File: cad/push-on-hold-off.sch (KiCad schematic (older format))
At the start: 13 parts, among them P1 CONN_01X04, P2 CONN_01X04, Q1 IRF7309IPBF, SW1 SW_PUSH_SMALL

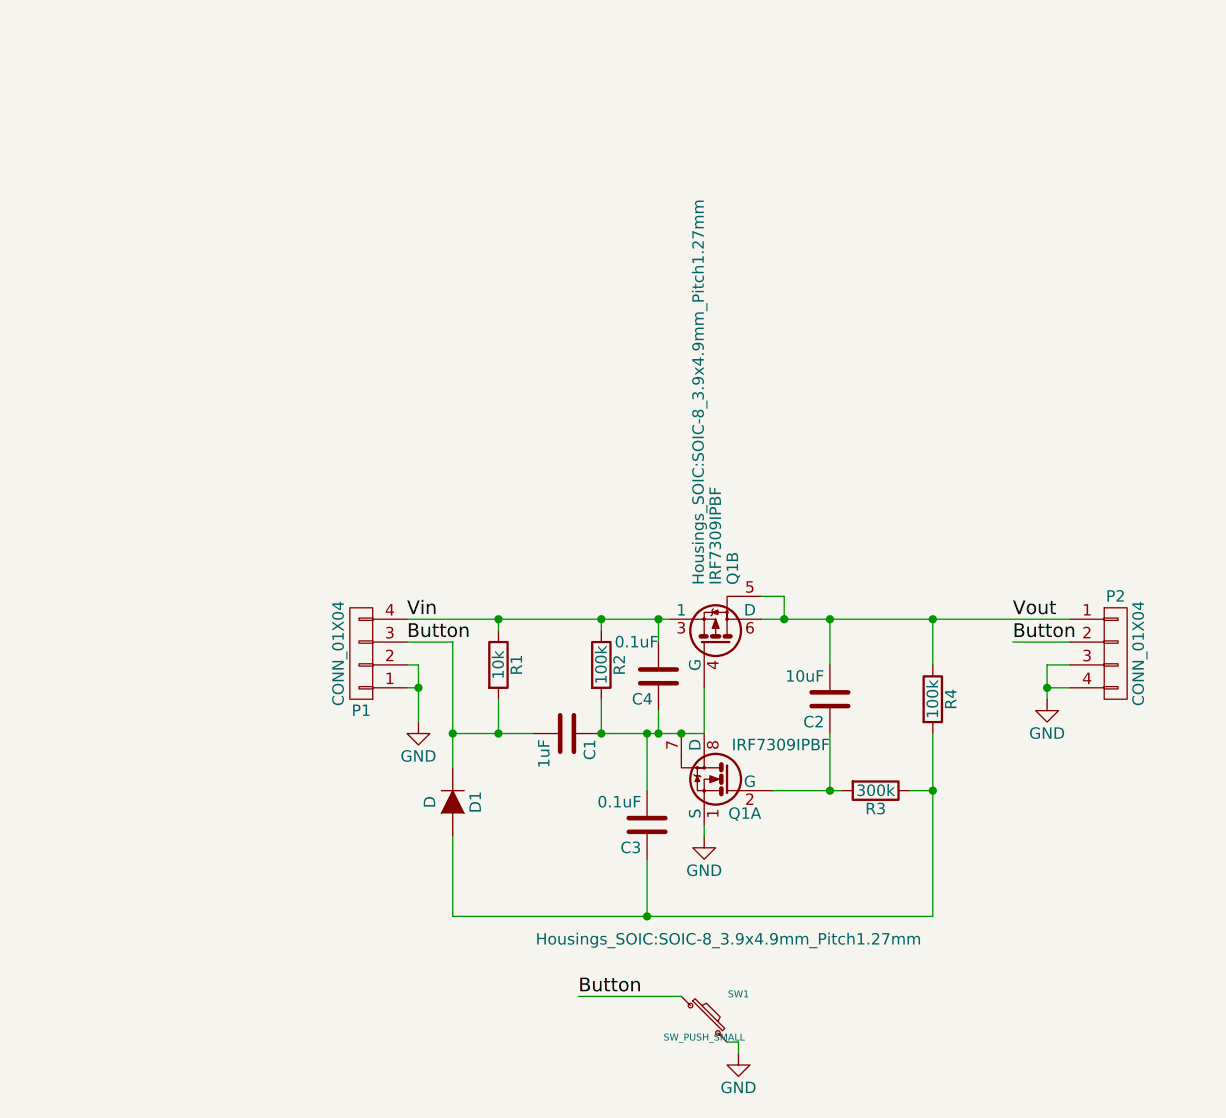
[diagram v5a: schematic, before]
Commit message: Add a jumper to configure auto on/off
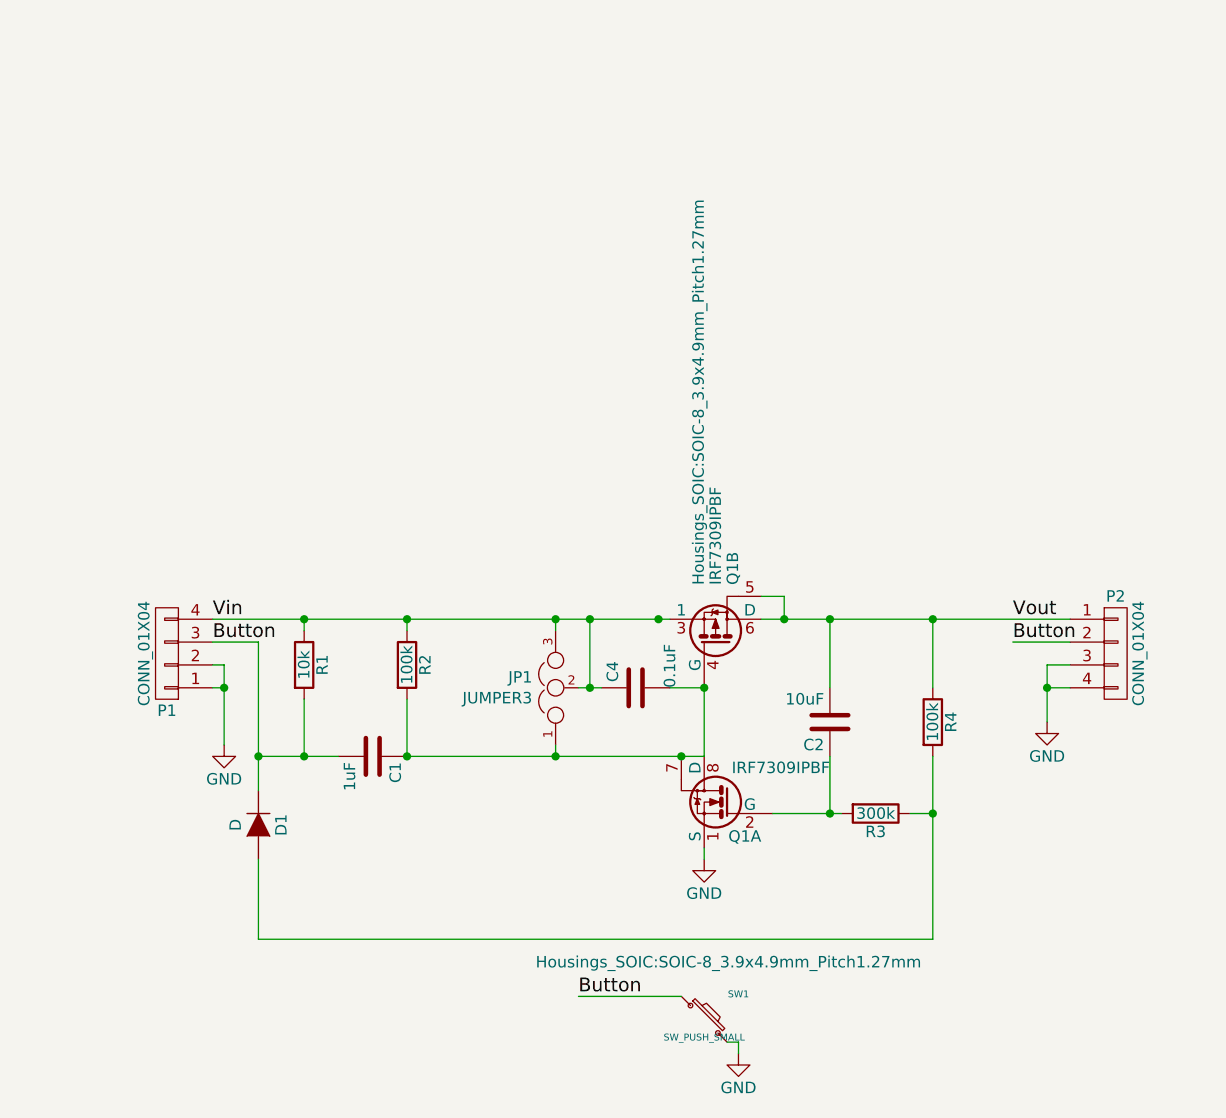
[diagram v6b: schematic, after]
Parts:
- removed C3: 0.1uF, Capacitors_SMD.pretty:C_0603_HandSoldering, symbol C
- added JP1: JUMPER3, mcous/kicad-lib/footprints/jumper.pretty:SOLDER-JUMPER_2-WAY, symbol JUMPER3
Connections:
- net Vin: now also C4.1, JP1.2, JP1.3; no longer C4.2
- net at C1.1, Q1.4 (G), Q1.7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: now also C4.2, JP1.1; no longer C4.1
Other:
- moved on the sheet: C1, C2, C4, D1, P1, Q1A, R1, R2, R3, R4

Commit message: Use custom footprint paths and add LEDs
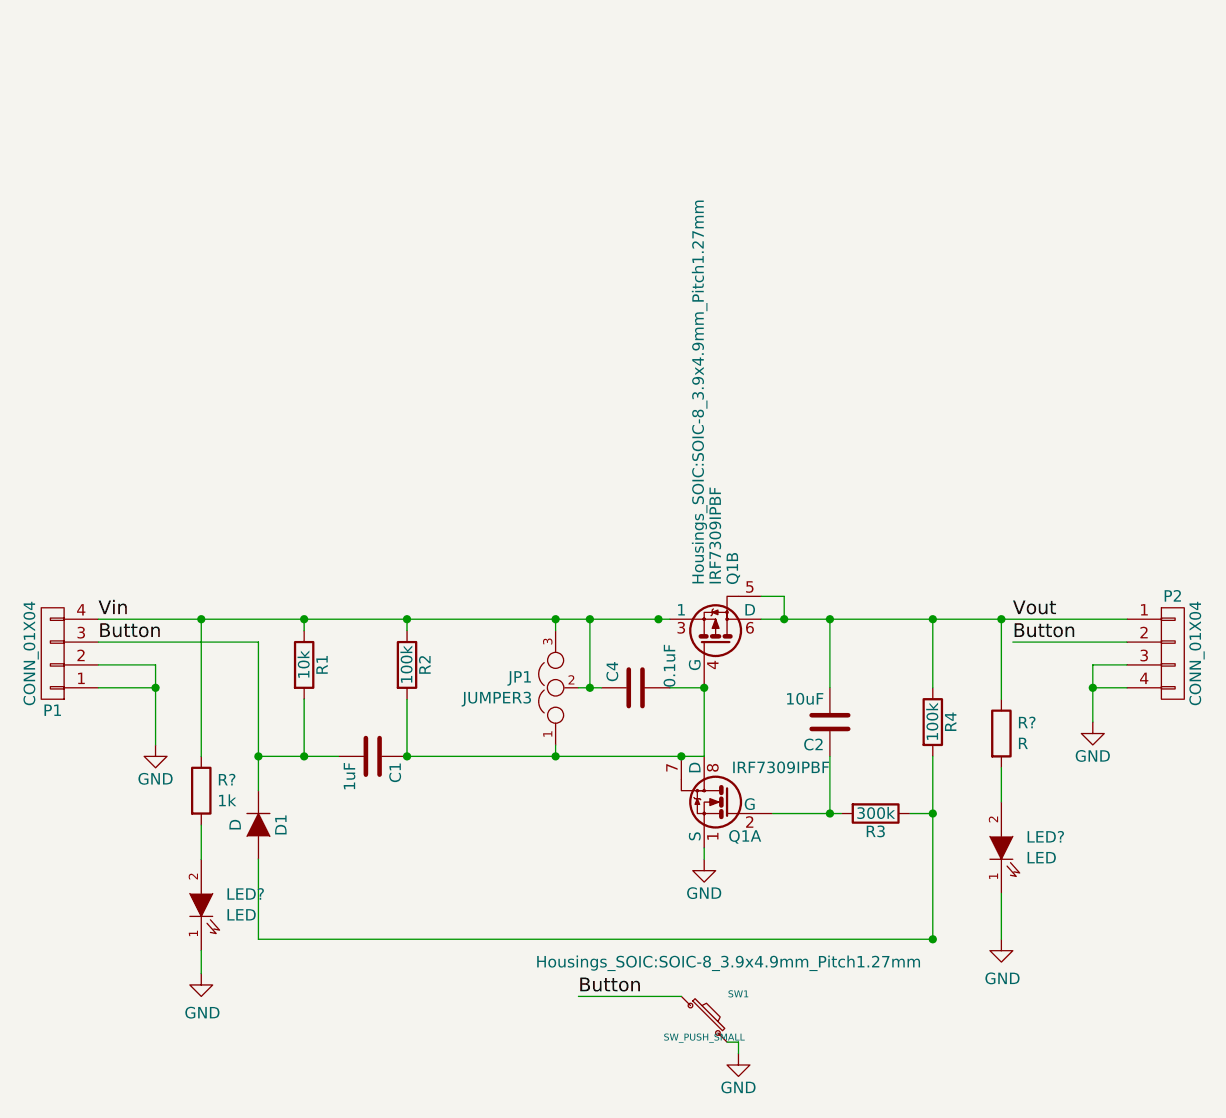
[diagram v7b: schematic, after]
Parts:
- added LED? (x2): LED, symbol LED
- added R?: R, symbol R
- added R?: 1k, symbol R
- C1, C2, C4: footprint Capacitors_SMD.pretty:C_0603_HandSoldering -> KiCad/Capacitors_SMD.pretty:C_0603_HandSoldering
- D1: footprint Diodes_SMD:SMA_Standard -> KiCad/Diodes_SMD.pretty:SMA_Handsoldering
- P1, P2: footprint Pin_Headers.pretty:Pin_Header_Straight_1x04 -> KiCad/Pin_Headers.pretty:Pin_Header_Straight_1x04
- R1, R2, R3, R4: footprint Resistors_SMD.pretty:R_0603_HandSoldering -> KiCad/Resistors_SMD.pretty:R_0603_HandSoldering
- SW1: footprint Buttons_Switches_SMD.pretty:SW_SPST_EVPBF -> KiCad/Buttons_Switches_SMD.pretty:SW_SPST_EVPBF
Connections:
- net GND: now also LED?.1 (K), LED?.1 (K)
- net Vin: now also R?.1
- net Vout: now also R?.1
- new net: LED?.2 (A), R?.2 (x2)
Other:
- moved on the sheet: P1, P2
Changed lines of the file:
@@
 L CONN_01X04 P1
 U 1 1 569FC392
-P 3600 3750
-F 0 "P1" H 3600 4000 50  0000 C CNN
-F 1 "CONN_01X04" V 3700 3750 50  0000 C CNN
-F 2 "Pin_Headers.pretty:Pin_Header_Straight_1x04" H 3600 3750 60  0001 C CNN
-F 3 "" H 3600 3750 60  0000 C CNN
-	1    3600 3750
+P 3100 3750
+F 0 "P1" H 3100 4000 50  0000 C CNN
+F 1 "CONN_01X04" V 3200 3750 50  0000 C CNN
+F 2 "KiCad/Pin_Headers.pretty:Pin_Header_Straight_1x04" H 3100 3750 60  0001 C CNN
+F 3 "" H 3100 3750 60  0000 C CNN
+	1    3100 3750
 	-1   0    0    1
 $EndComp
@@
 F 0 "R1" V 4280 3800 50  0000 C CNN
 F 1 "10k" V 4200 3800 50  0000 C CNN
-F 2 "Resistors_SMD.pretty:R_0603_HandSoldering" V 4130 3800 30  0001 C CNN
+F 2 "KiCad/Resistors_SMD.pretty:R_0603_HandSoldering" V 4130 3800 30  0001 C CNN
 F 3 "" H 4200 3800 30  0000 C CNN
 	1    4200 3800
@@
 F 0 "R2" V 4730 3800 50  0000 C CNN
 F 1 "100k" V 4650 3800 50  0000 C CNN
-F 2 "Resistors_SMD.pretty:R_0603_HandSoldering" V 4580 3800 30  0001 C CNN
+F 2 "KiCad/Resistors_SMD.pretty:R_0603_HandSoldering" V 4580 3800 30  0001 C CNN
 F 3 "" H 4650 3800 30  0000 C CNN
 	1    4650 3800
@@
 F 0 "C1" H 4525 4300 50  0000 L CNN
 F 1 "1uF" H 4525 4100 50  0000 L CNN
-F 2 "Capacitors_SMD.pretty:C_0603_HandSoldering" H 4538 4050 30  0001 C CNN
+F 2 "KiCad/Capacitors_SMD.pretty:C_0603_HandSoldering" H 4538 4050 30  0001 C CNN
 F 3 "" H 4500 4200 60  0000 C CNN
 	1    4500 4200
@@
 L GND #PWR01
 U 1 1 569FC7CE
-P 3850 4150
-F 0 "#PWR01" H 3850 3900 50  0001 C CNN
-F 1 "GND" H 3850 4000 50  0000 C CNN
-F 2 "" H 3850 4150 60  0000 C CNN
-F 3 "" H 3850 4150 60  0000 C CNN
-	1    3850 4150
-	1    0    0    -1
-$EndComp
-Text Label 3800 3700 0    60   ~ 0
+P 3550 4150
+F 0 "#PWR01" H 3550 3900 50  0001 C CNN
+F 1 "GND" H 3550 4000 50  0000 C CNN
+F 2 "" H 3550 4150 60  0000 C CNN
+F 3 "" H 3550 4150 60  0000 C CNN
+	1    3550 4150
+	1    0    0    -1
+$EndComp
+Text Label 3300 3700 0    60   ~ 0
 Button
 $Comp
@@
 F 0 "D1" H 4000 4600 50  0000 C CNN
 F 1 "D" H 4000 4400 50  0000 C CNN
-F 2 "Diodes_SMD:SMA_Standard" H 4000 4500 60  0001 C CNN
+F 2 "KiCad/Diodes_SMD.pretty:SMA_Handsoldering" H 4000 4500 60  0001 C CNN
 F 3 "" H 4000 4500 60  0000 C CNN
 F 4 "1466524" H 4000 4500 60  0001 C CNN "Vendor"
@@
 F 0 "C2" H 6525 4150 50  0000 L CNN
 F 1 "10uF" H 6525 3950 50  0000 L CNN
-F 2 "Capacitors_SMD.pretty:C_0603_HandSoldering" H 6538 3900 30  0001 C CNN
+F 2 "KiCad/Capacitors_SMD.pretty:C_0603_HandSoldering" H 6538 3900 30  0001 C CNN
 F 3 "" H 6500 4050 60  0000 C CNN
 	1    6500 4050
@@
 L CONN_01X04 P2
 U 1 1 569FCF63
-P 7750 3750
-F 0 "P2" H 7750 4000 50  0000 C CNN
-F 1 "CONN_01X04" V 7850 3750 50  0000 C CNN
-F 2 "Pin_Headers.pretty:Pin_Header_Straight_1x04" H 7750 3750 60  0001 C CNN
-F 3 "" H 7750 3750 60  0000 C CNN
-	1    7750 3750
+P 8000 3750
+F 0 "P2" H 8000 4000 50  0000 C CNN
+F 1 "CONN_01X04" V 8100 3750 50  0000 C CNN
+F 2 "KiCad/Pin_Headers.pretty:Pin_Header_Straight_1x04" H 8000 3750 60  0001 C CNN
+F 3 "" H 8000 3750 60  0000 C CNN
+	1    8000 3750
 	1    0    0    -1
 $EndComp
@@
 F 0 "R4" V 7030 4050 50  0000 C CNN
 F 1 "100k" V 6950 4050 50  0000 C CNN
-F 2 "Resistors_SMD.pretty:R_0603_HandSoldering" V 6880 4050 30  0001 C CNN
+F 2 "KiCad/Resistors_SMD.pretty:R_0603_HandSoldering" V 6880 4050 30  0001 C CNN
 F 3 "" H 6950 4050 30  0000 C CNN
 	1    6950 4050
@@
 F 0 "R3" V 6780 4450 50  0000 C CNN
 F 1 "300k" V 6700 4450 50  0000 C CNN
-F 2 "Resistors_SMD.pretty:R_0603_HandSoldering" V 6630 4450 30  0001 C CNN
+F 2 "KiCad/Resistors_SMD.pretty:R_0603_HandSoldering" V 6630 4450 30  0001 C CNN
 F 3 "" H 6700 4450 30  0000 C CNN
 	1    6700 4450
@@
 Text Label 7300 3600 0    60   ~ 0
 Vout
-Text Label 3800 3600 0    60   ~ 0
+Text Label 3300 3600 0    60   ~ 0
 Vin
 Text Label 7300 3700 0    60   ~ 0
@@
 L GND #PWR03
 U 1 1 569FDE5F
-P 7450 4050
-F 0 "#PWR03" H 7450 3800 50  0001 C CNN
-F 1 "GND" H 7450 3900 50  0000 C CNN
-F 2 "" H 7450 4050 60  0000 C CNN
-F 3 "" H 7450 4050 60  0000 C CNN
-	1    7450 4050
+P 7650 4050
+F 0 "#PWR03" H 7650 3800 50  0001 C CNN
+F 1 "GND" H 7650 3900 50  0000 C CNN
+F 2 "" H 7650 4050 60  0000 C CNN
+F 3 "" H 7650 4050 60  0000 C CNN
+	1    7650 4050
 	1    0    0    -1
 $EndComp
@@
 F 0 "SW1" H 6100 5460 30  0000 C CNN
 F 1 "SW_PUSH_SMALL" H 5950 5271 30  0000 C CNN
-F 2 "Buttons_Switches_SMD.pretty:SW_SPST_EVPBF" H 5950 5350 60  0001 C CNN
+F 2 "KiCad/Buttons_Switches_SMD.pretty:SW_SPST_EVPBF" H 5950 5350 60  0001 C CNN
 F 3 "" H 5950 5350 60  0000 C CNN
 F 4 "3801305" H 5950 5350 60  0001 C CNN "Vendor"
@@
 F 0 "C4" H 5675 4000 50  0000 L CNN
 F 1 "0.1uF" H 5650 3750 50  0000 L CNN
-F 2 "Capacitors_SMD.pretty:C_0603_HandSoldering" H 5688 3750 30  0001 C CNN
+F 2 "KiCad/Capacitors_SMD.pretty:C_0603_HandSoldering" H 5688 3750 30  0001 C CNN
 F 3 "" H 5650 3900 60  0000 C CNN
 	1    5650 3900
@@
 $EndComp
 Wire Wire Line
-	3800 3600 5800 3600
+	3300 3600 5800 3600
 Wire Wire Line
 	4200 3650 4200 3600
@@
 	5950 4200 5950 3900
 Wire Wire Line
-	3800 3800 3850 3800
-Wire Wire Line
-	3850 3800 3850 4150
-Wire Wire Line
-	3800 3900 3850 3900
-Connection ~ 3850 3900
-Wire Wire Line
-	3800 3700 4000 3700
+	3300 3800 3550 3800
+Wire Wire Line
+	3550 3800 3550 4150
+Wire Wire Line
+	3300 3900 3550 3900
+Connection ~ 3550 3900
+Wire Wire Line
+	3300 3700 4000 3700
 Wire Wire Line
 	4000 3700 4000 4350
@@
 	6500 3600 6500 3900
 Wire Wire Line
-	6200 3600 7550 3600
+	6200 3600 7800 3600
 Wire Wire Line
 	6300 3600 6300 3500
@@
 Connection ~ 6500 3600
 Wire Wire Line
-	6950 5000 6950 4200
+	6950 4200 6950 5000
 Connection ~ 6500 4450
 Wire Wire Line
@@
 Connection ~ 6950 3600
 Wire Wire Line
-	7550 3700 7300 3700
-Wire Wire Line
-	7550 3900 7450 3900
-Wire Wire Line
-	7450 3800 7450 4050
-Wire Wire Line
-	7550 3800 7450 3800
-Connection ~ 7450 3900
+	7800 3700 7300 3700
+Wire Wire Line
+	7800 3900 7650 3900
+Wire Wire Line
+	7650 3800 7650 4050
+Wire Wire Line
+	7800 3800 7650 3800
+Connection ~ 7650 3900
 Wire Wire Line
 	4000 4650 4000 5000
@@
 	5950 3900 5800 3900
 Wire Wire Line
-	5500 3900 5400 3900
+	5400 3900 5500 3900
 Connection ~ 5950 3900
 Wire Wire Line
@@
 Connection ~ 5450 3900
 Connection ~ 5450 3600
+$Comp
+L LED LED?
+U 1 1 57594F96
+P 7250 4600
+F 0 "LED?" V 7296 4492 50  0000 R CNN
+F 1 "LED" V 7205 4492 50  0000 R CNN
+F 2 "" H 7250 4600 50  0000 C CNN
+F 3 "" H 7250 4600 50  0000 C CNN
+	1    7250 4600
+	0    -1   -1   0
+$EndComp
+Wire Wire Line
+	7250 5000 7250 4800
+Connection ~ 6950 5000
+$Comp
+L R R?
+U 1 1 57595185
+P 7250 4100
+F 0 "R?" H 7320 4146 50  0000 L CNN
+F 1 "R" H 7320 4055 50  0000 L CNN
+F 2 "" V 7180 4100 50  0000 C CNN
+F 3 "" H 7250 4100 50  0000 C CNN
+	1    7250 4100
+	1    0    0    -1
+$EndComp
+Wire Wire Line
+	7250 3950 7250 3600
+Connection ~ 7250 3600
+Wire Wire Line
+	7250 4250 7250 4400
+$Comp
+L LED LED?
+U 1 1 5759593F
+P 3750 4850
+F 0 "LED?" V 3796 4742 50  0000 R CNN
+F 1 "LED" V 3705 4742 50  0000 R CNN
+F 2 "" H 3750 4850 50  0000 C CNN
+F 3 "" H 3750 4850 50  0000 C CNN
+	1    3750 4850
+	0    -1   -1   0
+$EndComp
+$Comp
+L R R?
+U 1 1 57595945
+P 3750 4350
+F 0 "R?" H 3820 4396 50  0000 L CNN
+F 1 "1k" H 3820 4305 50  0000 L CNN
+F 2 "" V 3680 4350 50  0000 C CNN
+F 3 "" H 3750 4350 50  0000 C CNN
+	1    3750 4350
+	1    0    0    -1
+$EndComp
+Wire Wire Line
+	3750 3600 3750 4200
+Wire Wire Line
+	3750 4500 3750 4650
+$Comp
+L GND #PWR?
+U 1 1 57595997
+P 7250 5000
+F 0 "#PWR?" H 7250 4750 50  0001 C CNN
+F 1 "GND" H 7255 4827 50  0000 C CNN
+F 2 "" H 7250 5000 50  0000 C CNN
+F 3 "" H 7250 5000 50  0000 C CNN
+	1    7250 5000
+	1    0    0    -1
+$EndComp
+$Comp
+L GND #PWR?
+U 1 1 575959DF
+P 3750 5150
+F 0 "#PWR?" H 3750 4900 50  0001 C CNN
+F 1 "GND" H 3755 4977 50  0000 C CNN
+F 2 "" H 3750 5150 50  0000 C CNN
+F 3 "" H 3750 5150 50  0000 C CNN
+	1    3750 5150
+	1    0    0    -1
+$EndComp
+Wire Wire Line
+	3750 5150 3750 5050
+Connection ~ 3750 3600
 $EndSCHEMATC

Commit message: Switch button footprint to match BOM
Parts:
- LED1, LED2: renamed from LED?; footprint (none) -> KiCad/LEDs.pretty:LED_0603
- R5: renamed from R?; footprint (none) -> KiCad/Resistors_SMD.pretty:R_0603_HandSoldering
- R6: renamed from R?; value R -> 1k; footprint (none) -> KiCad/Resistors_SMD.pretty:R_0603_HandSoldering
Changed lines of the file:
@@
 $EndComp
 $Comp
-L GND #PWR01
+L GND #PWR1
 U 1 1 569FC7CE
 P 3550 4150
-F 0 "#PWR01" H 3550 3900 50  0001 C CNN
+F 0 "#PWR1" H 3550 3900 50  0001 C CNN
 F 1 "GND" H 3550 4000 50  0000 C CNN
 F 2 "" H 3550 4150 60  0000 C CNN
@@
 $EndComp
 $Comp
-L GND #PWR02
+L GND #PWR3
 U 1 1 569FCD58
 P 5950 4650
-F 0 "#PWR02" H 5950 4400 50  0001 C CNN
+F 0 "#PWR3" H 5950 4400 50  0001 C CNN
 F 1 "GND" H 5950 4500 50  0000 C CNN
 F 2 "" H 5950 4650 60  0000 C CNN
@@
 Button
 $Comp
-L GND #PWR03
+L GND #PWR6
 U 1 1 569FDE5F
 P 7650 4050
-F 0 "#PWR03" H 7650 3800 50  0001 C CNN
+F 0 "#PWR6" H 7650 3800 50  0001 C CNN
 F 1 "GND" H 7650 3900 50  0000 C CNN
 F 2 "" H 7650 4050 60  0000 C CNN
@@
 $EndComp
 $Comp
-L GND #PWR04
+L GND #PWR4
 U 1 1 569FECE2
 P 6100 5500
-F 0 "#PWR04" H 6100 5250 50  0001 C CNN
+F 0 "#PWR4" H 6100 5250 50  0001 C CNN
 F 1 "GND" H 6100 5350 50  0000 C CNN
 F 2 "" H 6100 5500 60  0000 C CNN
@@
 Connection ~ 5450 3600
 $Comp
-L LED LED?
+L LED LED2
 U 1 1 57594F96
 P 7250 4600
-F 0 "LED?" V 7296 4492 50  0000 R CNN
+F 0 "LED2" V 7296 4492 50  0000 R CNN
 F 1 "LED" V 7205 4492 50  0000 R CNN
-F 2 "" H 7250 4600 50  0000 C CNN
+F 2 "KiCad/LEDs.pretty:LED_0603" H 7250 4600 50  0001 C CNN
 F 3 "" H 7250 4600 50  0000 C CNN
 	1    7250 4600
@@
 Connection ~ 6950 5000
 $Comp
-L R R?
+L R R6
 U 1 1 57595185
 P 7250 4100
-F 0 "R?" H 7320 4146 50  0000 L CNN
-F 1 "R" H 7320 4055 50  0000 L CNN
-F 2 "" V 7180 4100 50  0000 C CNN
+F 0 "R6" H 7320 4146 50  0000 L CNN
+F 1 "1k" H 7320 4055 50  0000 L CNN
+F 2 "KiCad/Resistors_SMD.pretty:R_0603_HandSoldering" V 7180 4100 50  0001 C CNN
 F 3 "" H 7250 4100 50  0000 C CNN
 	1    7250 4100
@@
 	7250 4250 7250 4400
 $Comp
-L LED LED?
+L LED LED1
 U 1 1 5759593F
 P 3750 4850
-F 0 "LED?" V 3796 4742 50  0000 R CNN
+F 0 "LED1" V 3796 4742 50  0000 R CNN
 F 1 "LED" V 3705 4742 50  0000 R CNN
-F 2 "" H 3750 4850 50  0000 C CNN
+F 2 "KiCad/LEDs.pretty:LED_0603" H 3750 4850 50  0001 C CNN
 F 3 "" H 3750 4850 50  0000 C CNN
 	1    3750 4850
@@
 $EndComp
 $Comp
-L R R?
+L R R5
 U 1 1 57595945
 P 3750 4350
-F 0 "R?" H 3820 4396 50  0000 L CNN
+F 0 "R5" H 3820 4396 50  0000 L CNN
 F 1 "1k" H 3820 4305 50  0000 L CNN
-F 2 "" V 3680 4350 50  0000 C CNN
+F 2 "KiCad/Resistors_SMD.pretty:R_0603_HandSoldering" V 3680 4350 50  0001 C CNN
 F 3 "" H 3750 4350 50  0000 C CNN
 	1    3750 4350
@@
 	3750 4500 3750 4650
 $Comp
-L GND #PWR?
+L GND #PWR5
 U 1 1 57595997
 P 7250 5000
-F 0 "#PWR?" H 7250 4750 50  0001 C CNN
+F 0 "#PWR5" H 7250 4750 50  0001 C CNN
 F 1 "GND" H 7255 4827 50  0000 C CNN
 F 2 "" H 7250 5000 50  0000 C CNN
@@
 $EndComp
 $Comp
-L GND #PWR?
+L GND #PWR2
 U 1 1 575959DF
 P 3750 5150
-F 0 "#PWR?" H 3750 4900 50  0001 C CNN
+F 0 "#PWR2" H 3750 4900 50  0001 C CNN
 F 1 "GND" H 3755 4977 50  0000 C CNN
 F 2 "" H 3750 5150 50  0000 C CNN
